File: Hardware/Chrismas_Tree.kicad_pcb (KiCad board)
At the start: 2 copper layers, 264.4 x 368.3 mm, 201 parts, among them J1 DNP, J2 USB_B_Micro, Q1 BC548, U1 PIC18F23K22

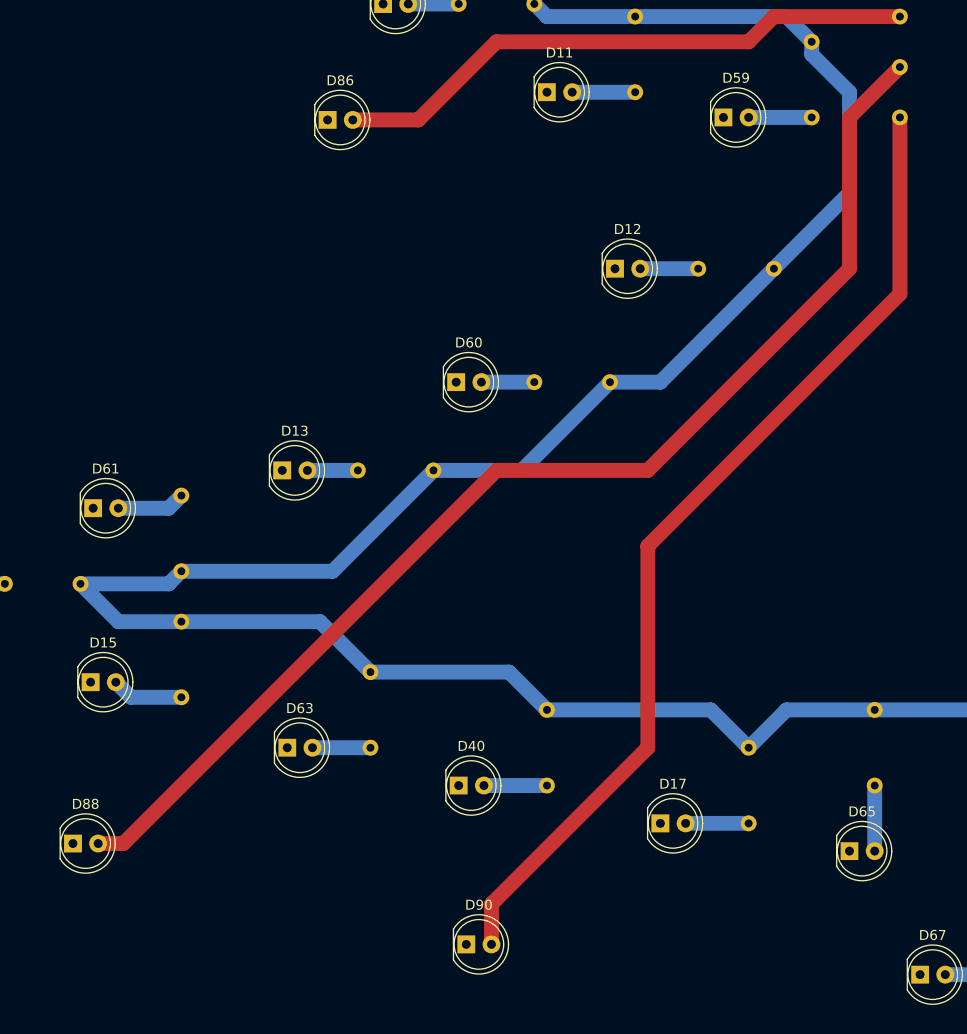
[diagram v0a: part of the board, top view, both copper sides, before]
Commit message: Adjusted bottom left branch light bulbs.
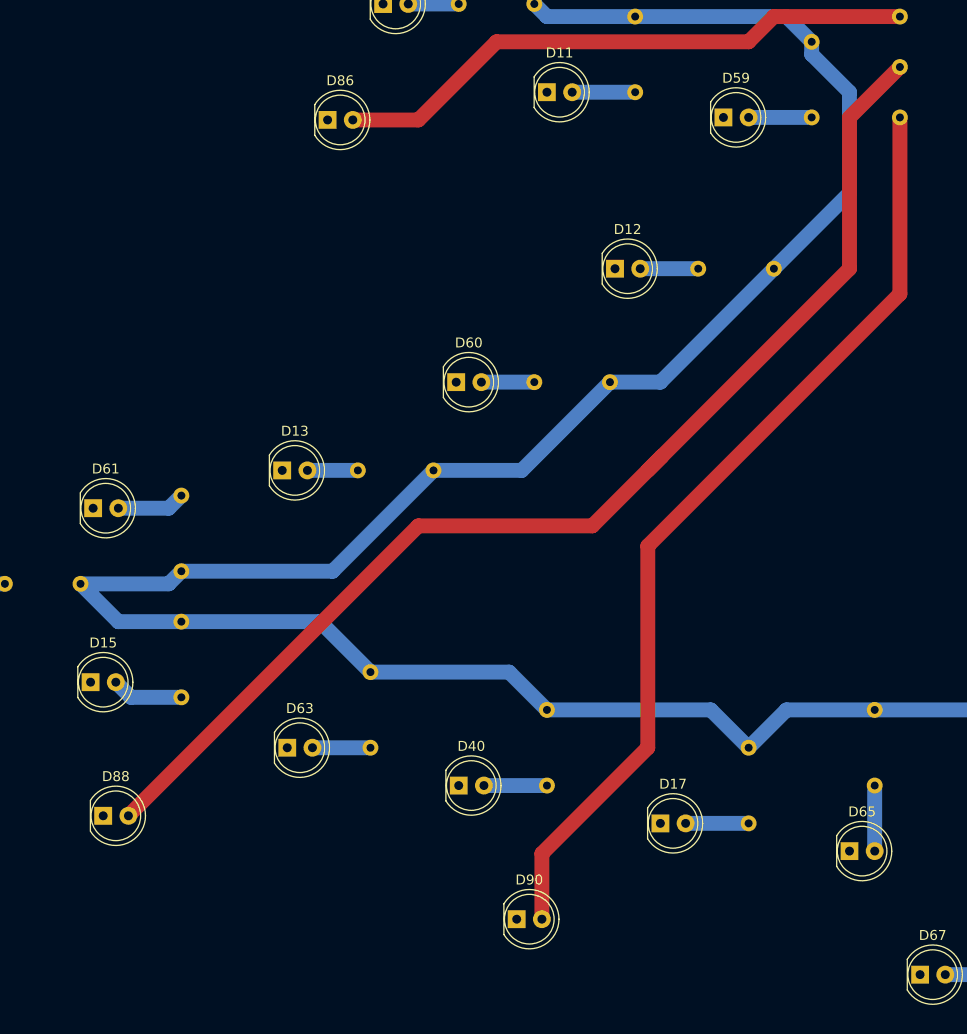
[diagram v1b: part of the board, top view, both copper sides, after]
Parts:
- moved D90 5.68 mm to (96.8, 329.9)
- moved D88 4.13 mm to (55.1, 319.5)
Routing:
- net Net-(D90-Pad2): track 100.4 -> 95.7 mm
- net Net-(D88-Pad2): track 122.1 -> 119.9 mm
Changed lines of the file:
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@@
     (thickness 1.6)
     (drawings 7)
-    (tracks 404)
+    (tracks 405)
     (zones 0)
     (modules 201)
@@
   )
   (setup
-    (last_trace_width 0.4)
+    (last_trace_width 1.5)
     (user_trace_width 0.4)
     (user_trace_width 1)
@@
   )
   (module LED_THT:LED_D5.0mm (layer F.Cu)
-    (at 91.694 332.486)
+    (at 96.774 329.946)
     (descr "LED, diameter 5.0mm, 2 pins, http://cdn-reichelt.de/documents/datenblatt/A500/LL-504BC2E-009.pdf")
     (tags "LED diameter 5.0mm 2 pins")
@@
   )
   (module LED_THT:LED_D5.0mm (layer F.Cu)
-    (at 52.07 322.326)
+    (at 55.118 319.532)
     (descr "LED, diameter 5.0mm, 2 pins, http://cdn-reichelt.de/documents/datenblatt/A500/LL-504BC2E-009.pdf")
     (tags "LED diameter 5.0mm 2 pins")
@@
   (segment (start 191.262 239.014) (end 188.722 236.474) (width 1.5) (layer F.Cu) (net 89))
   (segment (start 191.262 251.714) (end 191.262 239.014) (width 1.5) (layer F.Cu) (net 89))
-  (segment (start 54.61 322.326) (end 57.15 322.326) (width 1.5) (layer F.Cu) (net 90))
-  (segment (start 94.742 284.734) (end 109.982 284.734) (width 1.5) (layer F.Cu) (net 90))
-  (segment (start 57.15 322.326) (end 94.742 284.734) (width 1.5) (layer F.Cu) (net 90))
-  (segment (start 109.982 284.734) (end 130.302 264.414) (width 1.5) (layer F.Cu) (net 90))
-  (segment (start 130.302 249.174) (end 135.382 244.094) (width 1.5) (layer F.Cu) (net 90))
-  (segment (start 130.302 264.414) (end 130.302 249.174) (width 1.5) (layer F.Cu) (net 90))
+  (segment (start 135.382 244.094) (end 130.302 249.174) (width 1.5) (layer F.Cu) (net 90))
+  (segment (start 130.302 249.174) (end 130.302 264.414) (width 1.5) (layer F.Cu) (net 90))
+  (segment (start 57.658 319.532) (end 86.868 290.322) (width 1.5) (layer F.Cu) (net 90))
+  (segment (start 104.394 290.322) (end 111.379 283.337) (width 1.5) (layer F.Cu) (net 90))
+  (segment (start 86.868 290.322) (end 104.394 290.322) (width 1.5) (layer F.Cu) (net 90))
+  (segment (start 130.302 264.414) (end 111.379 283.337) (width 1.5) (layer F.Cu) (net 90))
+  (segment (start 111.379 283.337) (end 109.982 284.734) (width 1.5) (layer F.Cu) (net 90))
   (segment (start 265.684 319.278) (end 265.684 315.976) (width 1.5) (layer F.Cu) (net 91))
   (segment (start 265.684 315.976) (end 262.382 312.674) (width 1.5) (layer F.Cu) (net 91))
@@
   (segment (start 219.202 289.814) (end 188.722 259.334) (width 1.5) (layer F.Cu) (net 91))
   (segment (start 231.902 289.814) (end 219.202 289.814) (width 1.5) (layer F.Cu) (net 91))
-  (segment (start 94.234 332.486) (end 94.234 328.422) (width 1.5) (layer F.Cu) (net 92))
-  (segment (start 94.234 328.422) (end 109.982 312.674) (width 1.5) (layer F.Cu) (net 92))
   (segment (start 109.982 312.674) (end 109.982 292.354) (width 1.5) (layer F.Cu) (net 92))
   (segment (start 135.382 266.954) (end 135.382 249.174) (width 1.5) (layer F.Cu) (net 92))
   (segment (start 109.982 292.354) (end 135.382 266.954) (width 1.5) (layer F.Cu) (net 92))
+  (segment (start 99.314 323.342) (end 99.314 329.946) (width 1.5) (layer F.Cu) (net 92))
+  (segment (start 109.982 312.674) (end 99.314 323.342) (width 1.5) (layer F.Cu) (net 92))
   (segment (start 224.028 328.165208) (end 224.282 327.911208) (width 1.5) (layer F.Cu) (net 93))
   (segment (start 224.028 329.438) (end 224.028 328.165208) (width 1.5) (layer F.Cu) (net 93))

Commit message: Added fixation holes to PCB.
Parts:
- added REF**: MountingHole_4.5mm_Pad, MountingHole:MountingHole_4.5mm_Pad, F.Cu at (278.1, 379.0)
- added REF**: MountingHole_4.5mm_Pad, MountingHole:MountingHole_4.5mm_Pad, F.Cu at (278.1, 209.8)
- added REF**: MountingHole_4.5mm_Pad, MountingHole:MountingHole_4.5mm_Pad, F.Cu at (278.1, 40.6)
- added REF**: MountingHole_4.5mm_Pad, MountingHole:MountingHole_4.5mm_Pad, F.Cu at (43.7, 40.6)
- added REF**: MountingHole_4.5mm_Pad, MountingHole:MountingHole_4.5mm_Pad, F.Cu at (43.7, 209.8)
- added REF**: MountingHole_4.5mm_Pad, MountingHole:MountingHole_4.5mm_Pad, F.Cu at (43.7, 379.0)
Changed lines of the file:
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@@
     (tracks 405)
     (zones 0)
-    (modules 201)
+    (modules 207)
     (nets 129)
   )
@@
     (mod_text_size 1 1)
     (mod_text_width 0.15)
-    (pad_size 1.524 1.524)
-    (pad_drill 0.762)
+    (pad_size 4.5 4.5)
+    (pad_drill 4.5)
     (pad_to_mask_clearance 0.051)
     (solder_mask_min_width 0.25)
@@
       (outputformat 1)
       (mirror false)
-      (drillshape 1)
+      (drillshape 0)
       (scaleselection 1)
       (outputdirectory ""))
@@
     (add_net "Net-(U1-Pad7)")
   )
+  (module MountingHole:MountingHole_4.5mm_Pad (layer F.Cu)
+    (at 278.13 378.968)
+    (descr "Mounting Hole 4.5mm")
+    (tags "mounting hole 4.5mm")
+    (attr virtual)
+    (fp_text reference REF** (at 0 -5.5) (layer F.SilkS) hide
+      (effects (font (size 1 1) (thickness 0.15)))
+    )
+    (fp_text value MountingHole_4.5mm_Pad (at 0 5.5) (layer F.Fab)
+      (effects (font (size 1 1) (thickness 0.15)))
+    )
+    (fp_text user %R (at 0.3 0) (layer F.Fab)
+      (effects (font (size 1 1) (thickness 0.15)))
+    )
+    (fp_circle (center 0 0) (end 4.5 0) (layer Cmts.User) (width 0.15))
+    (fp_circle (center 0 0) (end 4.75 0) (layer F.CrtYd) (width 0.05))
+    (pad 1 thru_hole circle (at 0 0) (size 9 9) (drill 4.5) (layers *.Cu *.Mask))
+  )
+  (module MountingHole:MountingHole_4.5mm_Pad (layer F.Cu)
+    (at 278.13 209.804)
+    (descr "Mounting Hole 4.5mm")
+    (tags "mounting hole 4.5mm")
+    (attr virtual)
+    (fp_text reference REF** (at 0 -5.5) (layer F.SilkS) hide
+      (effects (font (size 1 1) (thickness 0.15)))
+    )
+    (fp_text value MountingHole_4.5mm_Pad (at 0 5.5) (layer F.Fab)
+      (effects (font (size 1 1) (thickness 0.15)))
+    )
+    (fp_circle (center 0 0) (end 4.75 0) (layer F.CrtYd) (width 0.05))
+    (fp_circle (center 0 0) (end 4.5 0) (layer Cmts.User) (width 0.15))
+    (fp_text user %R (at 0.3 0) (layer F.Fab)
+      (effects (font (size 1 1) (thickness 0.15)))
+    )
+    (pad 1 thru_hole circle (at 0 0) (size 9 9) (drill 4.5) (layers *.Cu *.Mask))
+  )
+  (module MountingHole:MountingHole_4.5mm_Pad (layer F.Cu)
+    (at 278.13 40.64)
+    (descr "Mounting Hole 4.5mm")
+    (tags "mounting hole 4.5mm")
+    (attr virtual)
+    (fp_text reference REF** (at 0 -5.5) (layer F.SilkS) hide
+      (effects (font (size 1 1) (thickness 0.15)))
+    )
+    (fp_text value MountingHole_4.5mm_Pad (at 0 5.5) (layer F.Fab)
+      (effects (font (size 1 1) (thickness 0.15)))
+    )
+    (fp_text user %R (at 0.3 0) (layer F.Fab)
+      (effects (font (size 1 1) (thickness 0.15)))
+    )
+    (fp_circle (center 0 0) (end 4.5 0) (layer Cmts.User) (width 0.15))
+    (fp_circle (center 0 0) (end 4.75 0) (layer F.CrtYd) (width 0.05))
+    (pad 1 thru_hole circle (at 0 0) (size 9 9) (drill 4.5) (layers *.Cu *.Mask))
+  )
+  (module MountingHole:MountingHole_4.5mm_Pad (layer F.Cu)
+    (at 43.688 40.64)
+    (descr "Mounting Hole 4.5mm")
+    (tags "mounting hole 4.5mm")
+    (attr virtual)
+    (fp_text reference REF** (at 0 -5.5) (layer F.SilkS) hide
+      (effects (font (size 1 1) (thickness 0.15)))
+    )
+    (fp_text value MountingHole_4.5mm_Pad (at 0 5.5) (layer F.Fab)
+      (effects (font (size 1 1) (thickness 0.15)))
+    )
+    (fp_circle (center 0 0) (end 4.75 0) (layer F.CrtYd) (width 0.05))
+    (fp_circle (center 0 0) (end 4.5 0) (layer Cmts.User) (width 0.15))
+    (fp_text user %R (at 0.3 0) (layer F.Fab)
+      (effects (font (size 1 1) (thickness 0.15)))
+    )
+    (pad 1 thru_hole circle (at 0 0) (size 9 9) (drill 4.5) (layers *.Cu *.Mask))
+  )
+  (module MountingHole:MountingHole_4.5mm_Pad (layer F.Cu)
+    (at 43.688 209.804)
+    (descr "Mounting Hole 4.5mm")
+    (tags "mounting hole 4.5mm")
+    (attr virtual)
+    (fp_text reference REF** (at 0 -5.5) (layer F.SilkS) hide
+      (effects (font (size 1 1) (thickness 0.15)))
+    )
+    (fp_text value MountingHole_4.5mm_Pad (at 0 5.5) (layer F.Fab)
+      (effects (font (size 1 1) (thickness 0.15)))
+    )
+    (fp_text user %R (at 0.3 0) (layer F.Fab)
+      (effects (font (size 1 1) (thickness 0.15)))
+    )
+    (fp_circle (center 0 0) (end 4.5 0) (layer Cmts.User) (width 0.15))
+    (fp_circle (center 0 0) (end 4.75 0) (layer F.CrtYd) (width 0.05))
+    (pad 1 thru_hole circle (at 0 0) (size 9 9) (drill 4.5) (layers *.Cu *.Mask))
+  )
+  (module MountingHole:MountingHole_4.5mm_Pad (layer F.Cu)
+    (at 43.688 378.968)
+    (descr "Mounting Hole 4.5mm")
+    (tags "mounting hole 4.5mm")
+    (attr virtual)
+    (fp_text reference REF** (at 0 -5.5) (layer F.SilkS) hide
+      (effects (font (size 1 1) (thickness 0.15)))
+    )
+    (fp_text value MountingHole_4.5mm_Pad (at 0 5.5) (layer F.Fab)
+      (effects (font (size 1 1) (thickness 0.15)))
+    )
+    (fp_circle (center 0 0) (end 4.75 0) (layer F.CrtYd) (width 0.05))
+    (fp_circle (center 0 0) (end 4.5 0) (layer Cmts.User) (width 0.15))
+    (fp_text user %R (at 0.3 0) (layer F.Fab)
+      (effects (font (size 1 1) (thickness 0.15)))
+    )
+    (pad 1 thru_hole circle (at 0 0) (size 9 9) (drill 4.5) (layers *.Cu *.Mask))
+  )
   (module Connector_USB:USB_Micro-B_Molex-105017-0001 (layer B.Cu)

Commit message: Increased transitor base resistor value.
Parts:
- R96: value 180 -> 220
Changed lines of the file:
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@@
       (drillshape 0)
       (scaleselection 1)
-      (outputdirectory ""))
+      (outputdirectory "Production_Files/"))
   )
   (net 0 "")
@@
       (effects (font (size 1 1) (thickness 0.15)) (justify mirror))
     )
-    (fp_text value 180 (at 3.81 -2.37 90) (layer B.Fab)
-      (effects (font (size 1 1) (thickness 0.15)) (justify mirror))
-    )
+    (fp_text value 220 (at 3.81 -2.37 90) (layer B.Fab)
+      (effects (font (size 1 1) (thickness 0.15)) (justify mirror))
+    )
